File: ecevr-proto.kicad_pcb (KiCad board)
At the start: 4 copper layers, 100 x 92 mm, 359 parts, among them J1 CUR_SEL, J19 SFP, J2 PEN_SEL, J20 SFP_CAGE, J2001 BNC, J2051 BNC, J2201 BEL_0845_2G1T_H5, J3 USB_C_Receptacle_USB2.0, J4 JTAG, Q1 SSM6N35AFE, Q2 SSM6N35AFE, Q3 Si3477, SW1 PROG, SW2101 SW_DIP_x08, U1 XC7A35T-CSG325, U10 74VHC1G03, U11 UTC2000, U12 5P49V6965, U13 TPS3808DBV, U14 74LVC1G06, U15 74LVC2T45DC, U16 74LVC2T45DC, U2 AT25SL641, U2001 74LVC2T45DC, U2051 74LVC2T45DC, U2101 74AHC1T86, U2102 74AHC1T86, U2103 PCA9306, U2104 24AA0x, U2105 74AHC1T86, U2106 74AHC1T86, U2201 74AHC1T86, U2202 74LVC1G06, U2301 lan9254, U2302 SN74LV1T34DBV, U3 FT240XQ, U4 TLV62569ADDC, U5 TPS62A01A-SOT563, U6 TPS62A01A-SOT563, U7 TLV62569ADDC, U8 74ALVC125, U9 TLV62569ADDC, X2301 FNETHE025, Y1 25MHz

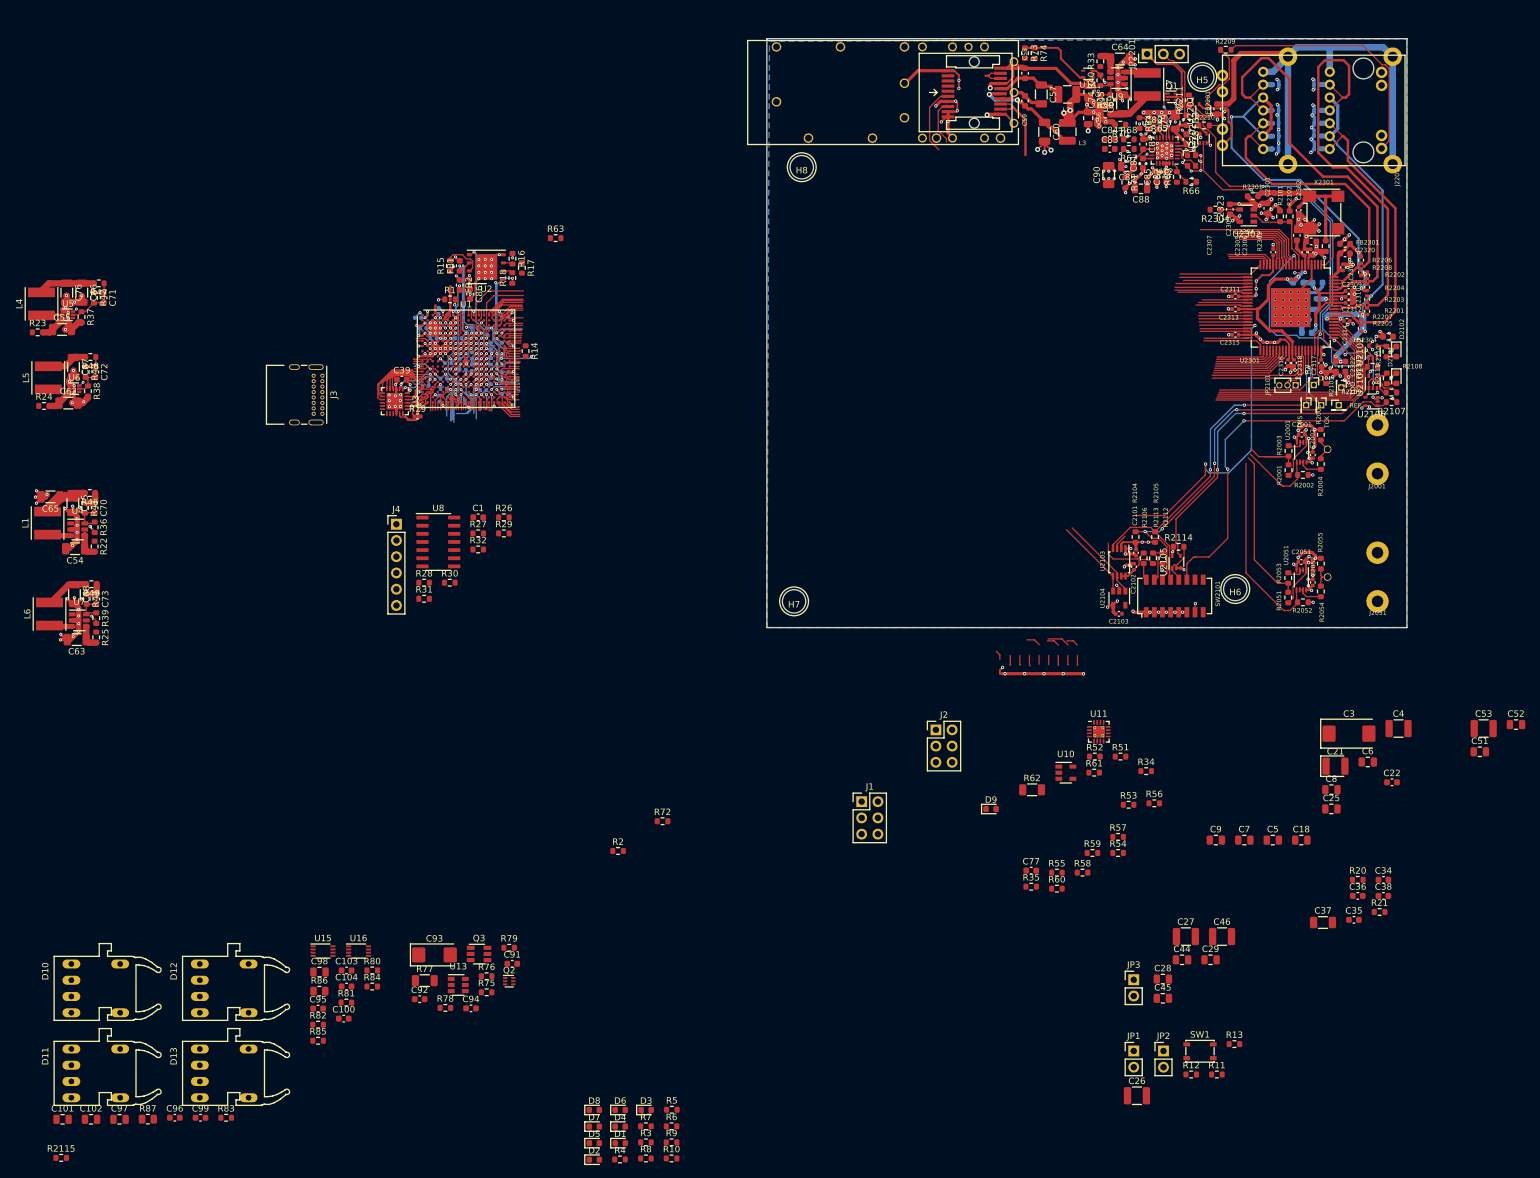
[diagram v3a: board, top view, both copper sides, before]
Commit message: re-routed with more relaxed specs (that eurocircuits can also meet)
No chance with OSH, however...

Going to place stuff on the board now...
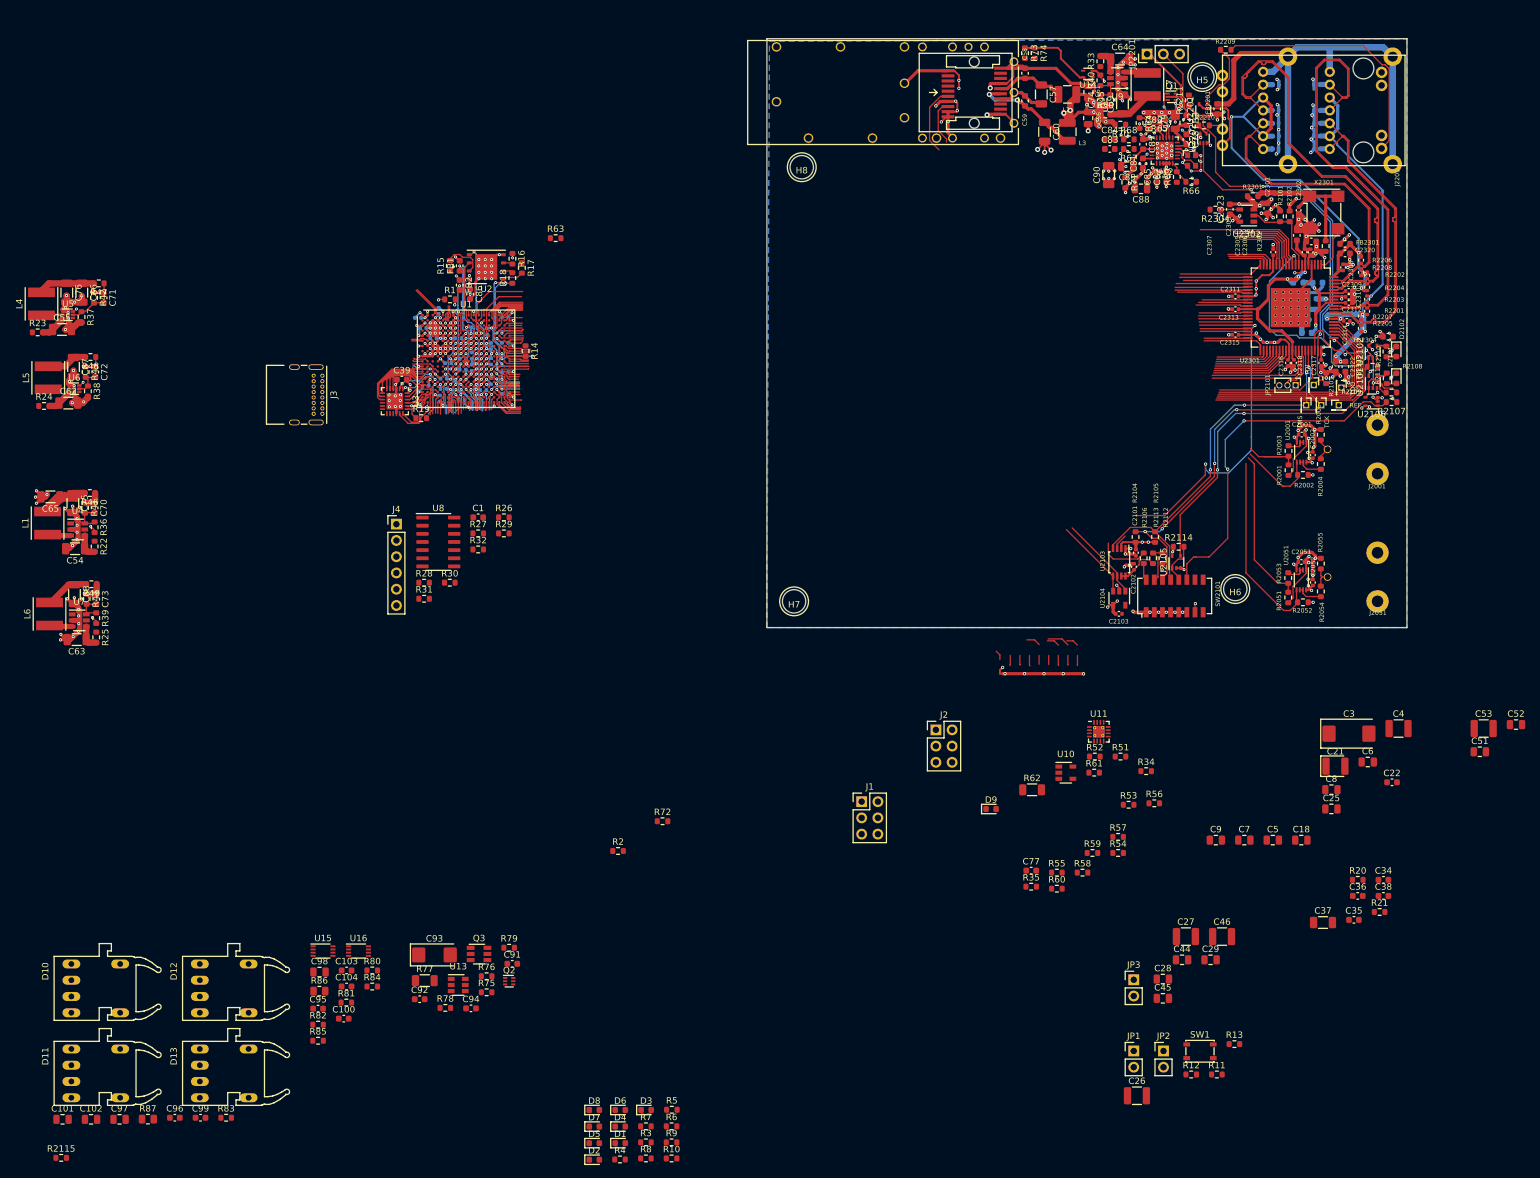
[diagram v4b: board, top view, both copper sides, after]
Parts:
- R19: footprint Resistor_SMD:R_0402_1005Metric -> Resistor_SMD:R_0603_1608Metric
- moved R19 0.64 mm to (46.0, 89.3)
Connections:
- R19 pad 1: IO_L12P_T1_MRCC_34 -> IO_L17P_T2_34
- U3 pad 19: IO_L12P_T1_MRCC_34 -> IO_L17P_T2_34
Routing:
- net IO_L17P_T2_34: track 0.00 -> 8.13 mm
- net MGT_RX1_N: track 12.4 -> 5.18 mm
- net MGT_RX1_P: track 12.4 -> 5.37 mm
- net IO_L19P_T3_34: track 0.00 -> 5.46 mm, vias 0 -> 1
- net GND: track 506.6 -> 511.4 mm, vias 312 -> 311
- net /lan9254/LINKACT0: track 66.4 -> 62.0 mm
- net IO_25_34: track 4.22 -> 0.00 mm
- net IO_L21N_T3_DQS_34: track 0.00 -> 3.50 mm
- net MGT_REFCLK_P: track 5.93 -> 2.55 mm
- net IO_L5N_T0_34: track 0.00 -> 3.29 mm
- net Net-(R17-Pad2): track 15.5 -> 18.7 mm
- net MGT_REFCLK_N: track 5.88 -> 2.70 mm
- net IO_L4P_T0_34: track 3.17 -> 0.00 mm
- net IO_L12P_T1_MRCC_34: track 8.33 -> 5.67 mm, vias 0 -> 1
- net TMS: track 6.83 -> 4.63 mm
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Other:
- net class Default: clearance 0.0889 -> 0.1; trace_width 0.0889 -> 0.1; via_dia 0.508 -> 0.46; via_drill 0.254 -> 0.2
- net class diffp removed
- net class diffp_ec removed
- net class eurockt_diff100 added: clearance 0.1, trace_width 0.116, via_dia 0.46, via_drill 0.2
- net class eurockt_se50 added: clearance 0.1, trace_width 0.182, via_dia 0.46, via_drill 0.2
- net class jlc_diff100 added: clearance 0.1, trace_width 0.102, via_dia 0.46, via_drill 0.2
- net class jlc_se50 added: clearance 0.1, trace_width 0.147, via_dia 0.46, via_drill 0.2
- rule trace_clearance: 0.0889 -> 0.1
- rule trace_min: 0.0889 -> 0.1

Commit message: further work...
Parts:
- removed D3, D4, D5, D6, D9: LED, LED_SMD:LED_0603_1608Metric
- removed R51: 1k, Resistor_SMD:R_0603_1608Metric
- removed R63: 4k7, Resistor_SMD:R_0603_1608Metric
- removed U2302: SN74LV1T34DBV, Package_TO_SOT_SMD:SOT-23-5
- added C105: 100nF, Capacitor_SMD:C_0603_1608Metric, F.Cu at (132.0, 73.8)
- added C106: 100nF_603, Capacitor_SMD:C_0603_1608Metric, F.Cu at (141.3, 91.3)
- added Q4: SSM6N35AFE, proj_footprints:SOT-563-adjusted, F.Cu at (108.9, 47.5)
- added Q5: SSM6N35AFE, proj_footprints:SOT-563-adjusted, F.Cu at (105.5, 47.7)
- added Q6: Si3477, Package_TO_SOT_SMD:TSOT-23-6, F.Cu at (114.9, 54.5)
- added Q7: SSM6N35AFE, proj_footprints:SOT-563-adjusted, F.Cu at (139.8, 83.2)
- added R100: 2k, Resistor_SMD:R_0603_1608Metric, F.Cu at (146.3, 33.3)
- added R2116: 0, Resistor_SMD:R_0603_1608Metric, F.Cu at (162.6, 108.2)
- added R2117: 0, Resistor_SMD:R_0603_1608Metric, F.Cu at (164.1, 107.2)
- added R2305: 0, Resistor_SMD:R_0603_1608Metric, F.Cu at (178.8, 81.8)
- added R2306: 10k, Resistor_SMD:R_0603_1608Metric, F.Cu at (138.2, 89.7)
- added R88: 4k7, Resistor_SMD:R_0603_1608Metric, F.Cu at (115.2, 48.9)
- added R89: 1k, Resistor_SMD:R_0603_1608Metric, F.Cu at (115.8, 77.9)
- added R90: 1k, Resistor_SMD:R_0603_1608Metric, F.Cu at (113.9, 72.9)
- added R91: 4k7, Resistor_SMD:R_0603_1608Metric, F.Cu at (115.2, 50.4)
- added R92: 47k, Resistor_SMD:R_0603_1608Metric, F.Cu at (118.6, 53.8)
- added R93: 47k, Resistor_SMD:R_0603_1608Metric, F.Cu at (118.6, 55.3)
- added R94: 47k, Resistor_SMD:R_0603_1608Metric, F.Cu at (123.2, 48.9)
- added R95: 47k, Resistor_SMD:R_0603_1608Metric, F.Cu at (123.2, 50.4)
- added R96: 47k, Resistor_SMD:R_0603_1608Metric, F.Cu at (122.2, 47.4)
- added R97: 47k, Resistor_SMD:R_0603_1608Metric, F.Cu at (125.2, 47.4)
- added R98: 230, Resistor_SMD:R_0603_1608Metric, F.Cu at (107.9, 49.2)
- added R99: 750, Resistor_SMD:R_0603_1608Metric, F.Cu at (110.9, 48.4)
- added TP1: Dummy End, proj_footprints:endpoint_0.1mm, B.Cu at (162.8, 62.8)
- added TP10: Dummy End, proj_footprints:endpoint_0.1mm, F.Cu at (155.1, 79.4)
- added TP11: Dummy End, proj_footprints:endpoint_0.1mm, B.Cu at (157.5, 79.0)
- added TP12: Dummy End, proj_footprints:endpoint_0.1mm, B.Cu at (157.7, 79.0)
- added TP13: Dummy End, proj_footprints:endpoint_0.1mm, B.Cu at (157.9, 79.0)
- added TP14: TestPoint, TestPoint:TestPoint_Pad_D1.0mm, F.Cu at (148.8, 32.9)
- added TP2: Dummy End, proj_footprints:endpoint_0.1mm, F.Cu at (163.1, 62.8)
- added TP3: Dummy End, proj_footprints:endpoint_0.1mm, B.Cu at (164.8, 62.3)
- added TP4: Dummy End, proj_footprints:endpoint_0.1mm, B.Cu at (164.4, 79.0)
- added TP5: Dummy End, proj_footprints:endpoint_0.1mm, F.Cu at (164.8, 79.0)
- added TP6: Dummy End, proj_footprints:endpoint_0.1mm, B.Cu at (163.9, 79.0)
- added TP7: Dummy End, proj_footprints:endpoint_0.1mm, F.Cu at (163.9, 79.0)
- added TP8: Dummy End, proj_footprints:endpoint_0.1mm, F.Cu at (164.3, 79.0)
- added U17: 74LVC06, Package_SO:TSSOP-14_4.4x5mm_P0.65mm, F.Cu at (132.3, 89.6)
- added U18: 74LVC1T126, Package_TO_SOT_SMD:SOT-23-5, F.Cu at (175.0, 57.6)
- added U19: 74AHC1T86, Package_TO_SOT_SMD:SOT-353_SC-70-5, F.Cu at (126.0, 73.7)
- added U20: 74AHC1T86, Package_TO_SOT_SMD:SOT-353_SC-70-5, F.Cu at (129.1, 73.7)
- added U21: 74LVC1G06, Package_TO_SOT_SMD:SOT-353_SC-70-5, F.Cu at (145.6, 35.4)
- added U22: 74AC126, Package_SO:TSSOP-14_4.4x5mm_P0.65mm, F.Cu at (146.6, 88.3)
- C18, C21, C25, C28, C29, C44, C45, C5, C51, C52, C6, C7, C8, C9: moved to B.Cu
- C22: footprint Capacitor_SMD:C_0603_1608Metric -> Capacitor_SMD:C_0402_1005Metric; moved to B.Cu
- D1, D2, D7, D8: value LED -> LED_BARG; footprint LED_SMD:LED_0603_1608Metric -> proj_footprints:LED_RGB_2504_horiz_barg
- J2: footprint Connector_PinHeader_2.54mm:PinHeader_2x03_P2.54mm_Vertical -> Connector_PinHeader_2.54mm:PinHeader_2x02_P2.54mm_Vertical
- J2001, J2051: footprint proj_footprints:BNC_Molex_0731713150 -> proj_footprints:LEMO+SMA
- R10, R3, R6: value 1k -> 750
- R15, R16, R17: value 2k4 -> 10k
- R2002, R2052: value 2k2 -> 3k3
- R2108: value 1k -> 10k
- R2110: value 100 -> 1k5
- R2111: value 100 -> 3k3
- R22, R23, R24, R25, R33: value 10k -> 100k
- R2209, R2210: value 100 -> 178
- R2211: value 100 -> 10k
- R4, R7, R9: value 1k -> 2k
- R40: value 45.9k -> 10k
- R45: value 10.2k -> 45k3
- R5, R8: value 1k -> 230
- R52, R76: value 100k -> 10k
- R66: value 1k78 -> 10k
- R75: value 100k -> 45.3k
- R77: value 47 -> 50; footprint Resistor_SMD:R_1206_3216Metric -> Resistor_SMD:R_0603_1608Metric
- R82, R83: value 1k -> 100k
- R84, R85: value 1k -> 4k7
- R86, R87: value 90 -> 100
- SW1: footprint Button_Switch_SMD:SW_SPST_PTS810 -> proj_footprints:SW_SPST_PTS810_and_PTS841
- U10: value 74VHC1G03 -> 74LVC1G06; footprint Package_TO_SOT_SMD:SOT-23-5 -> Package_TO_SOT_SMD:SOT-353_SC-70-5
- U14, U2202: footprint proj_footprints:SOT-5x3 -> Package_TO_SOT_SMD:SOT-353_SC-70-5
- U2104: value 24AA0x -> 24FC16T
- U8: footprint Package_SO:SOIC-14_3.9x8.7mm_P1.27mm -> Package_SO:TSSOP-14_4.4x5mm_P0.65mm
- X2301: footprint Oscillator:Oscillator_SMD_Diodes_FN-4Pin_7.0x5.0mm -> proj_footprints:FNETH_and_ASE-4Pin_3.2x2.5mm
- moved R2115 186.8 mm to (156.2, 119.9)
- moved C101 184.8 mm to (114.1, 61.9), turned to 90 degrees
- moved R82 182.5 mm to (163.6, 59.8)
- moved D11 181.0 mm to (110.0, 55.0), turned to 180 degrees
- moved R83 179.5 mm to (154.1, 84.4)
- moved C97 174.1 mm to (118.3, 72.2)
- moved C96 169.2 mm to (121.8, 73.8), turned to 90 degrees
- moved C102 169.0 mm to (114.1, 79.5), turned to 90 degrees
- moved C99 165.6 mm to (115.8, 70.0), turned to 90 degrees
- moved R87 165.3 mm to (114.1, 76.1), turned to 270 degrees
- moved D10 164.0 mm to (110.0, 65.2), turned to 180 degrees
- moved C65 163.3 mm to (146.8, 63.2), turned to 90 degrees
- moved R85 163.2 mm to (115.2, 47.4), turned to 180 degrees
- moved L1 161.0 mm to (142.8, 62.8), turned to 0 degrees
- moved C75 158.4 mm to (145.9, 66.7), turned to 180 degrees
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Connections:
- C101 pad 1: +5V -> +5V_SWITCHED
- C102 pad 1: +5V -> +5V_SWITCHED
- C103 pad 2: +5V -> +5V_SWITCHED
- C104 pad 2: +5V -> +5V_SWITCHED
- D1 pad 1: GND -> Net-(D1-Pad1)
- D1 pad 2: Net-(D1-Pad2) -> +5V
- D10 pad 3: +5V -> +5V_SWITCHED
- D12 pad 3: +5V -> +5V_SWITCHED
- D2 pad 1: GND -> Net-(D2-Pad1)
- D2 pad 2: Net-(D2-Pad2) -> +5V
- D7 pad 1: GND -> Net-(D7-Pad1)
- D7 pad 2: Net-(D7-Pad2) -> +5V
- D8 pad 1: GND -> Net-(D8-Pad1)
- D8 pad 2: Net-(D8-Pad2) -> +5V
- J19 pad 2: IO_L7N_T1_AD2N_15 -> Net-(J19-Pad2)
- J19 pad 6: IO_L5N_T0_AD9N_15 -> Net-(J19-Pad6)
- J19 pad 8: IO_L4N_T0_15 -> Net-(J19-Pad8)
- J2 pad 2: USB_BCDb -> Net-(J2-Pad2)
- J2 pad 3: Net-(J2-Pad1) -> Net-(J2-Pad3)
- J2 pad 4: IO_L15N_T2_DQS_34 -> Net-(J2-Pad2)
- Q1 pad 1: IO_L7P_T1_AD2P_15 -> IO_L4N_T0_15
- Q2 pad 3: Net-(Q2-Pad3) -> Net-(J2-Pad2)
- R10 pad 1: IO_L20P_T3_34 -> Net-(D7-Pad3)
- R10 pad 2: Net-(D8-Pad2) -> Net-(Q5-Pad3)
- R2 pad 2: IO_L23N_T3_A02_D18_14 -> IO_L23P_T3_A03_D19_14
- R2107 pad 1: +3V3 -> GND
- R2108 pad 2: Net-(R2108-Pad2) -> IO_L22P_T3_A05_D21_14
- R2112 pad 1: IO_L21P_T3_DQS_14 -> IO_L23N_T3_A02_D18_14
- R2113 pad 2: IO_L21P_T3_DQS_14 -> IO_L23N_T3_A02_D18_14
- R2114 pad 1: +1V8 -> GND
- R2114 pad 2: IO_L22P_T3_A05_D21_14 -> Net-(R2114-Pad2)
- R3 pad 1: IO_L3P_T0_DQS_34 -> Net-(R3-Pad1)
- R3 pad 2: Net-(D1-Pad2) -> Net-(D1-Pad3)
- R35 pad 1: Net-(R35-Pad1) -> USB_BCDb
- R35 pad 2: +5V -> GND
- R4 pad 1: IO_L3N_T0_DQS_34 -> Net-(R4-Pad1)
- R4 pad 2: Net-(D2-Pad2) -> Net-(D1-Pad4)
- R5 pad 1: IO_L18N_T2_34 -> Net-(R5-Pad1)
- R5 pad 2: Net-(D3-Pad2) -> Net-(D1-Pad1)
- R52 pad 1: Net-(J2-Pad1) -> IO_L15N_T2_DQS_34
- R52 pad 2: +5V -> GND
- R6 pad 1: IO_L18P_T2_34 -> Net-(R6-Pad1)
- R6 pad 2: Net-(D4-Pad2) -> Net-(D2-Pad3)
- R64 pad 1: IO_L7P_T1_AD2P_15 -> IO_L4N_T0_15
- R7 pad 1: IO_25_34 -> Net-(R7-Pad1)
- R7 pad 2: Net-(D5-Pad2) -> Net-(D2-Pad4)
- R72 pad 2: IO_L23P_T3_A03_D19_14 -> IO_L21P_T3_DQS_14
- R8 pad 1: IO_L20N_T3_34 -> Net-(R8-Pad1)
- R8 pad 2: Net-(D6-Pad2) -> Net-(D2-Pad1)
- R80 pad 1: IO_L22P_T3_34 -> IO_L4P_T0_34
- R81 pad 1: IO_L22N_T3_34 -> IO_L4N_T0_34
- R82 pad 1: IO_L24N_T3_34 -> +1V8
- R82 pad 2: GND -> Net-(R82-Pad2)
- R83 pad 1: IO_L24P_T3_34 -> +1V8
- R83 pad 2: GND -> TDO
- R84 pad 1: IO_L24N_T3_34 -> /CFG_DONE
- R84 pad 2: Net-(D10-Pad1) -> +1V8
- R85 pad 1: IO_L24P_T3_34 -> Net-(J19-Pad2)
- R85 pad 2: Net-(D12-Pad1) -> +3V3
- R9 pad 1: IO_L23N_T3_34 -> Net-(D7-Pad4)
- R9 pad 2: Net-(D7-Pad2) -> Net-(Q5-Pad6)
- SW1 pad 1: Net-(R12-Pad1) -> GND
- SW1 pad 2: GND -> Net-(R12-Pad1)
- SW2101 pad 10: IO_L21N_T3_DQS_A06_D22_14 -> IO_L22N_T3_A04_D20_14
- SW2101 pad 12: IO_L22P_T3_A05_D21_14 -> Net-(R2114-Pad2)
- SW2101 pad 15: IO_L21P_T3_DQS_14 -> IO_L23N_T3_A02_D18_14
- SW2101 pad 5: GND -> +1V8
- SW2101 pad 6: GND -> +1V8
- SW2101 pad 9: IO_L22N_T3_A04_D20_14 -> IO_L21N_T3_DQS_A06_D22_14
- U1 pad F12: Net-(R63-Pad1) -> /CFG_DONE
- U1 pad K16: Net-(U1-PadK16) -> Net-(R82-Pad2)
- U10 pad 2: Net-(J2-Pad1) -> Net-(J1-Pad1)
- U12 pad 9: IO_L7P_T1_AD2P_15 -> IO_L4N_T0_15
- U13 pad 3: Net-(Q2-Pad3) -> Net-(J2-Pad2)
- U14 pad 1: Net-(U14-Pad1) -> +3V3
- U14 pad 2: IO_L5P_T0_AD9P_15 -> +3V3
- U14 pad 4: /SFP Connector/TX_DISABLE -> Net-(R100-Pad2)
- U15 pad 6: IO_L22P_T3_34 -> IO_L4P_T0_34
- U15 pad 7: IO_L22P_T3_34 -> IO_L4P_T0_34
- U16 pad 6: IO_L22N_T3_34 -> IO_L4N_T0_34
- U16 pad 7: IO_L22N_T3_34 -> IO_L4N_T0_34
- U2 pad 5: Net-(U1-PadK16) -> Net-(R82-Pad2)
- U2102 pad 1: Net-(R2108-Pad2) -> IO_L22P_T3_A05_D21_14
- U2103 pad 5: IO_L23N_T3_A02_D18_14 -> IO_L23P_T3_A03_D19_14
- U2103 pad 6: IO_L23P_T3_A03_D19_14 -> IO_L21P_T3_DQS_14
- U2104 pad 1: IO_L23P_T3_A03_D19_14 -> IO_L21P_T3_DQS_14
- U2104 pad 3: IO_L23N_T3_A02_D18_14 -> IO_L23P_T3_A03_D19_14
- U2105 pad 1: IO_L22P_T3_A05_D21_14 -> +1V8
- U2105 pad 2: GND -> Net-(R2114-Pad2)
- U2105 pad 4: Net-(R2108-Pad2) -> IO_L22P_T3_A05_D21_14
- U2106 pad 1: Net-(R2107-Pad2) -> +3V3
- U2106 pad 2: GND -> Net-(R2107-Pad2)
- U2202 pad 1: Net-(U2202-Pad1) -> /lan9254/LINKACT1
- U2301 pad 41: IO_L7P_T1_D09_14 -> IO_L7N_T1_D10_14
- U2301 pad 42: IO_L7N_T1_D10_14 -> IO_L7P_T1_D09_14
- U8 pad 13: GND -> /LAN9254_JTAG_EN
- U8 pad 2: TCK_I -> TMS_I
- U8 pad 3: TCK -> TMS
- U8 pad 5: TDI_I -> TCK_I
- U8 pad 6: TDI -> TCK
- U8 pad 8: TMS -> TDI
- U8 pad 9: TMS_I -> TDI_I
- U9 pad 5: Net-(R35-Pad1) -> Net-(TP14-Pad1)
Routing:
- net GND: track 511.4 -> 693.5 mm, vias 311 -> 392
- net +1V8: track 159.3 -> 333.8 mm, vias 74 -> 120
- net +5V: track 19.4 -> 133.1 mm, vias 0 -> 55
- net Net-(D8-Pad4): track 0.00 -> 101.5 mm, vias 0 -> 2
- net Net-(R12-Pad1): track 5.25 -> 99.5 mm, vias 1 -> 3
- net IO_L22P_T3_A05_D21_14: track 10.0 -> 93.1 mm, vias 1 -> 6
- net +5V_SWITCHED: track 0.00 -> 72.5 mm, vias 0 -> 4
- net Net-(R34-Pad2): track 0.00 -> 72.4 mm
- net /CFG_DONE: track 0.00 -> 72.1 mm, vias 0 -> 2
- net IO_L3P_T0_DQS_34: track 2.40 -> 74.3 mm
- net IO_L3N_T0_DQS_34: track 1.58 -> 72.4 mm
- net SDA1_3V3: track 0.86 -> 64.1 mm, vias 0 -> 2
- net +1V0: track 33.4 -> 96.1 mm, vias 22 -> 42
- net IO_L12P_T1_MRCC_34: track 5.67 -> 67.8 mm, vias 1 -> 4
- net /LAN9254_JTAG_EN: track 0.00 -> 61.8 mm, vias 0 -> 4
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- added copper zone on In2.Cu, net +5V
- added copper zone on F.Cu, net VBUS
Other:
- board text added: "A|I|EMUL|F|J|K"
- board text added: "EtherCat EVR V1.1.0"
- board text added: "GND"
- board text added: "REF 1V8"
- board text added: "TCK"
- board text added: "TDI"
- board text added: "TDO"
- board text added: "TMS"
- board text removed: "EtherCat / Zynq Development Board V1.0.0"

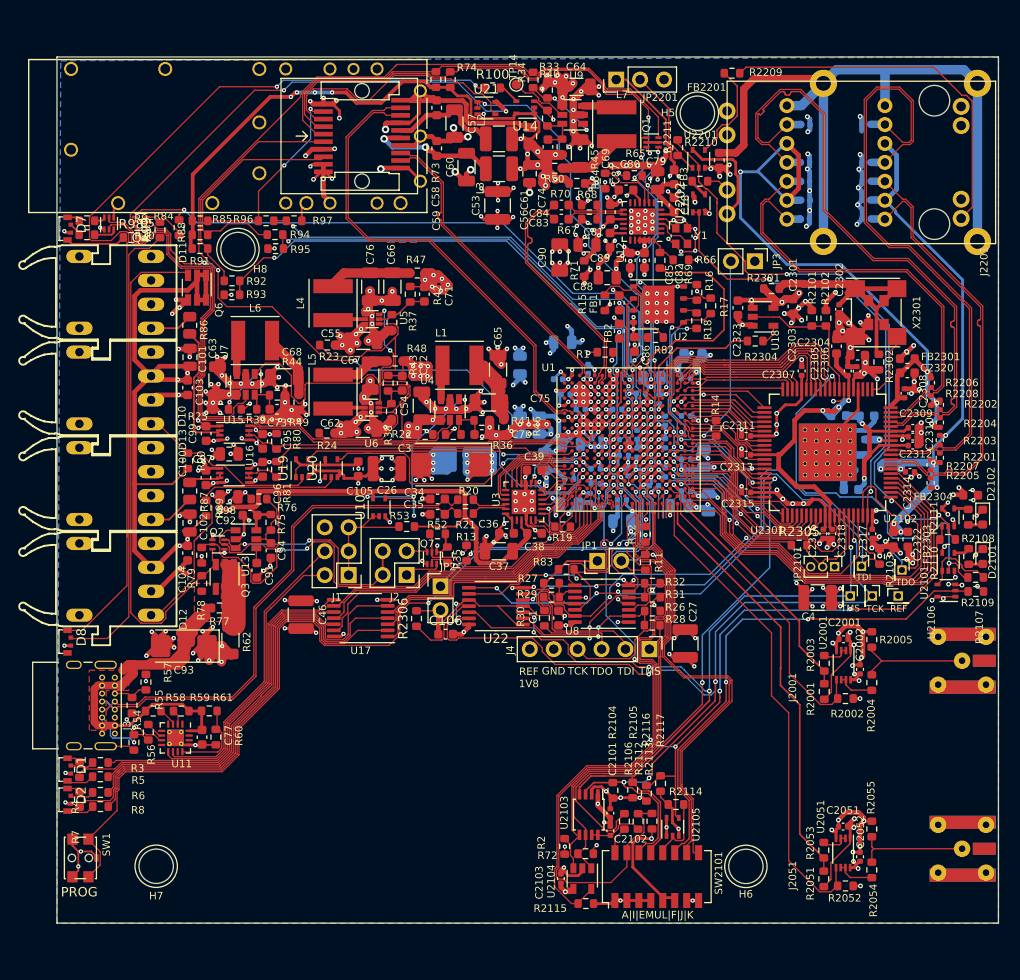
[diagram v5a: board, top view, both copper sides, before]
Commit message: pcb: increased board width to 100mmx100mm
In case we ever use an extruded Al box.
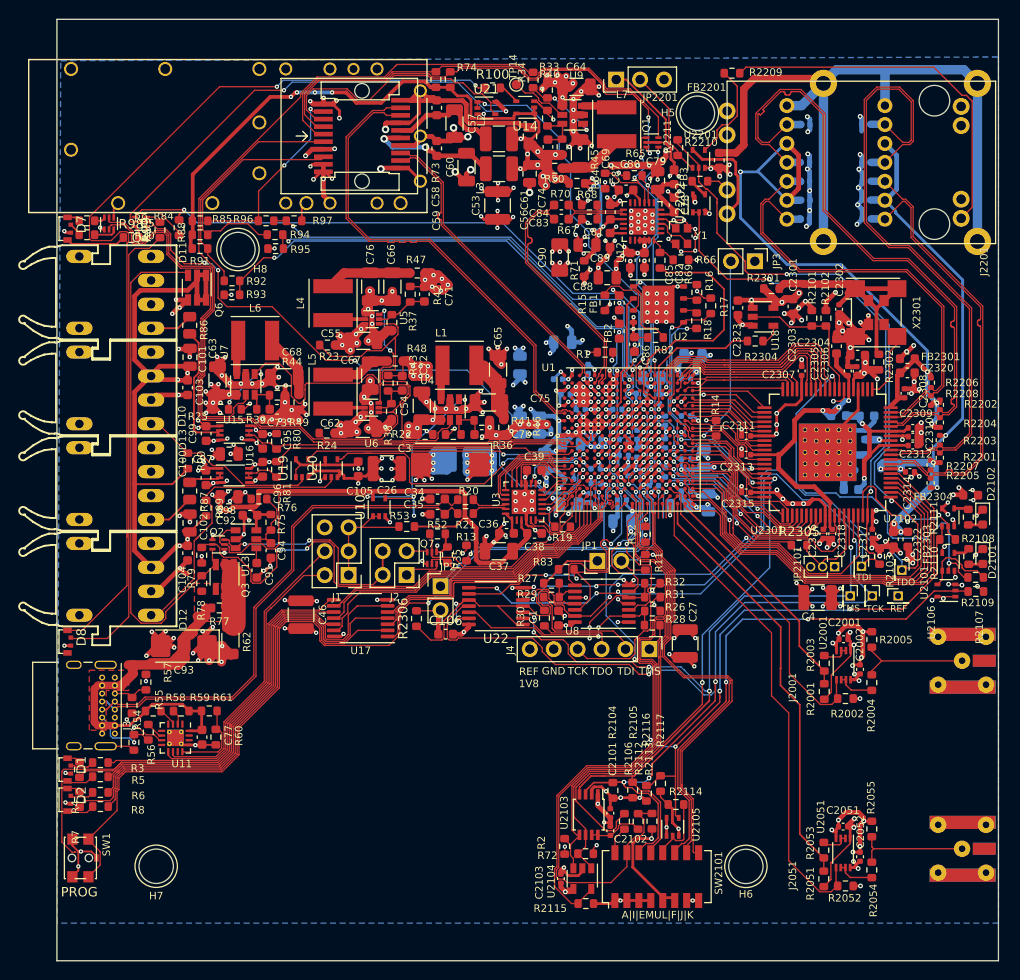
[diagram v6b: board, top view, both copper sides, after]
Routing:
- net Net-(R4-Pad1): track 40.1 -> 56.8 mm
- net VBUS: track 49.7 -> 45.6 mm
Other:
- board size 100 x 92 mm -> 100 x 100 mm
